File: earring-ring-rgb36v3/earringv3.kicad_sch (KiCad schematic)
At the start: 58 parts, among them J1 Conn_01x05, Q1 AO3401A, SW1 SW_Push, SW2 SW_Push, U1 GMA2718H09-F42-4P, U2 STM32L031G6Ux

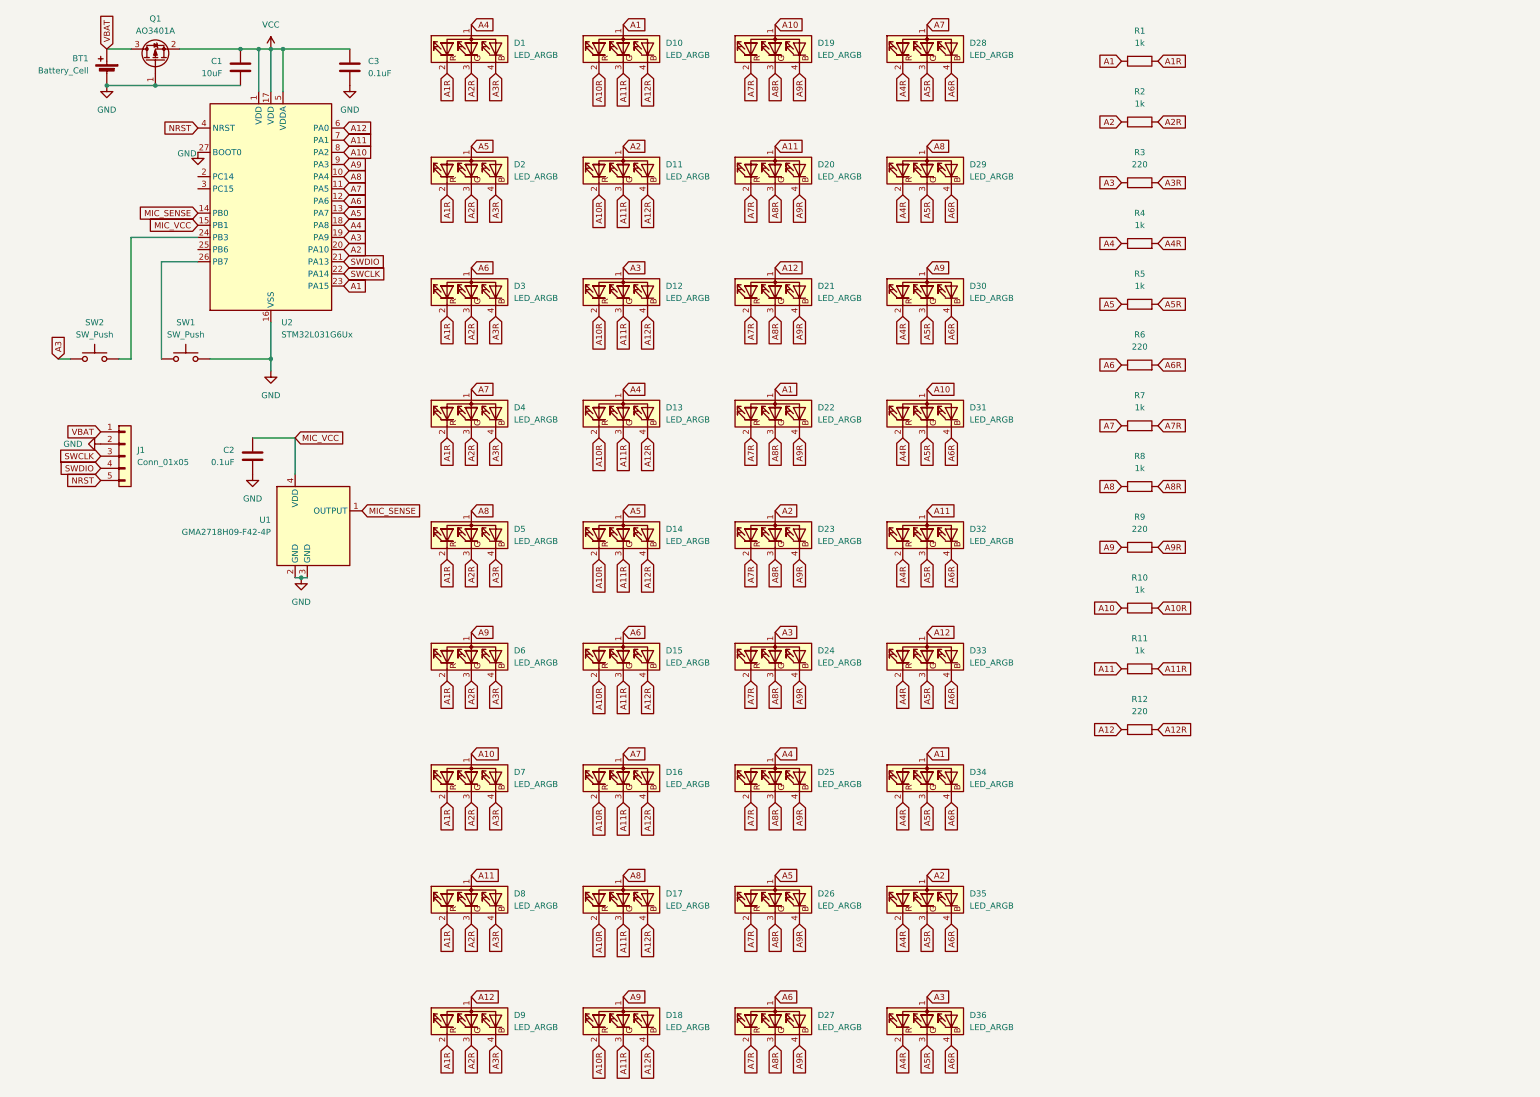
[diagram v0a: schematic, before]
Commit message: earring-ring-rgb36v3: schematic design for charlieplexing
This is the 3rd or 4th attempt, but the current schematic finally looks
usable.
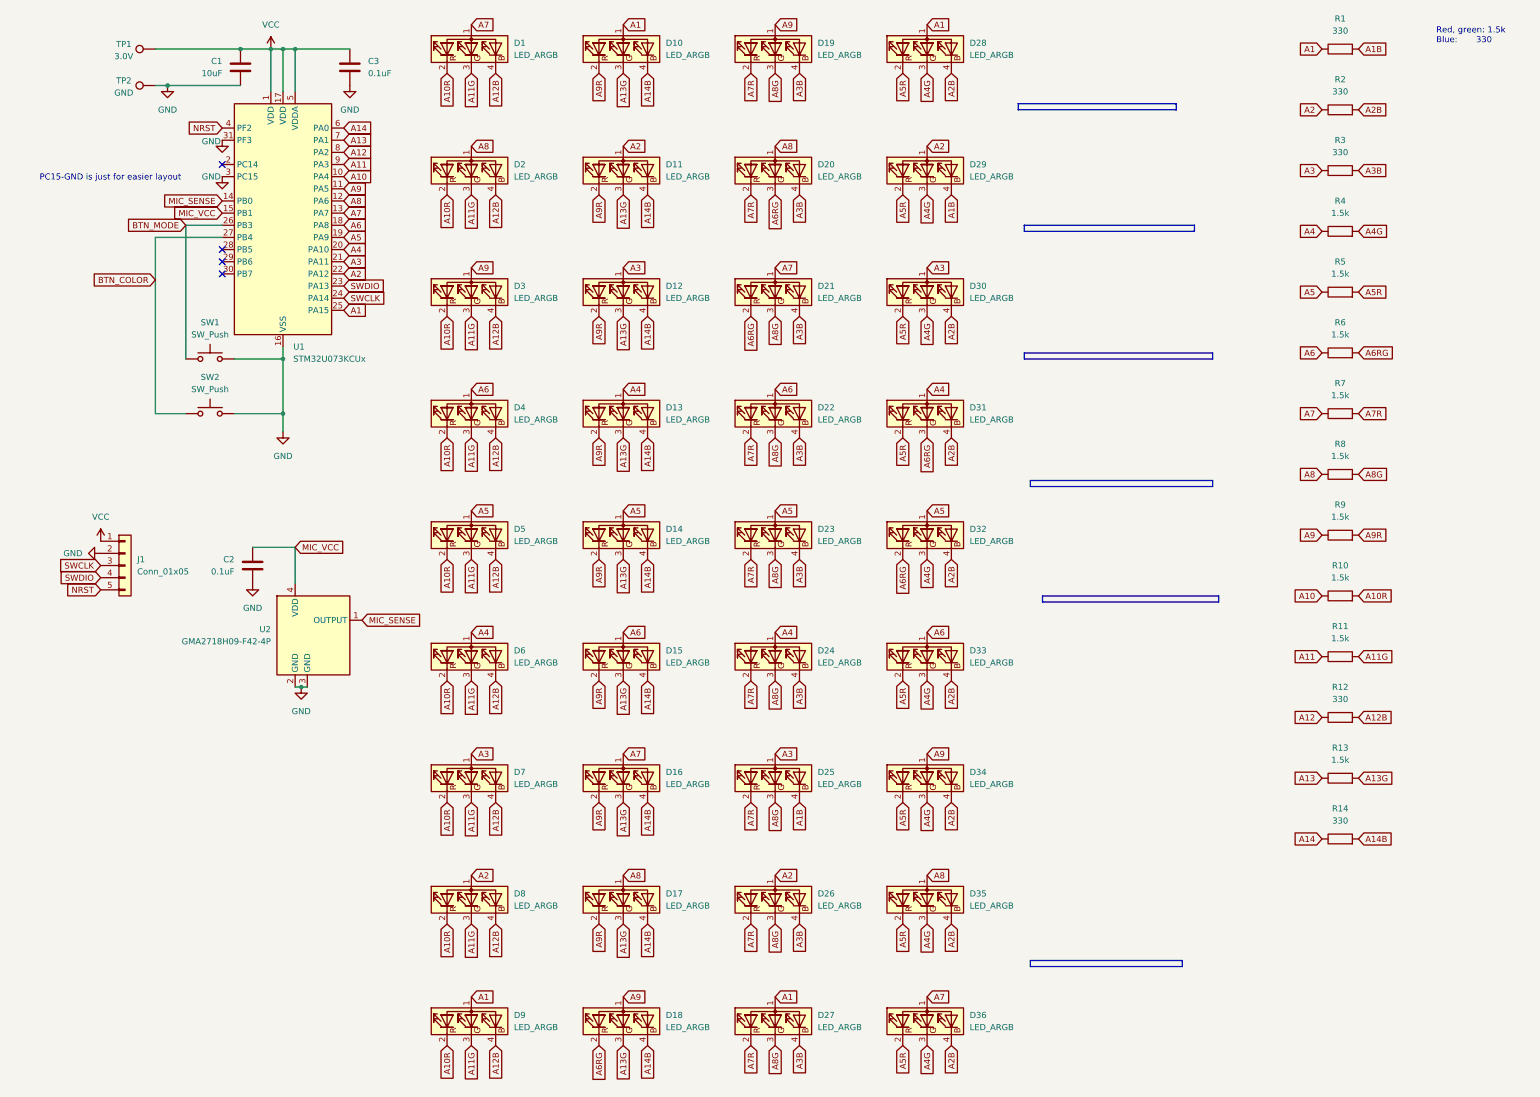
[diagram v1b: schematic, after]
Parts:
- removed BT1: Battery_Cell, Custom:MY-1220-03, symbol Device:Battery_Cell
- removed Q1: AO3401A, Package_TO_SOT_SMD:SOT-23, symbol Transistor_FET:AO3401A
- removed U2: STM32L031G6Ux, Package_DFN_QFN:QFN-28_4x4mm_P0.5mm, symbol MCU_ST_STM32L0:STM32L031G6Ux
- added R13: 1.5k, Resistor_SMD:R_0402_1005Metric, symbol Device:R
- added R14: 330, Resistor_SMD:R_0402_1005Metric, symbol Device:R
- added TP1: 3.0V, TestPoint:TestPoint_Pad_1.5x1.5mm, symbol Connector:TestPoint
- added TP2: GND, TestPoint:TestPoint_Pad_1.5x1.5mm, symbol Connector:TestPoint
- added U1: STM32U073KCUx, Package_DFN_QFN:QFN-32-1EP_5x5mm_P0.5mm_EP3.45x3.45mm, symbol MCU_ST_STM32U0:STM32U073KCUx
- R1, R2: value 1k -> 330; LCSC C11702 -> C25104
- R10, R11, R4, R5, R7, R8: value 1k -> 1.5k; LCSC C11702 -> C25867
- R12, R3: value 220 -> 330; LCSC C25091 -> C25104
- R6, R9: value 220 -> 1.5k; LCSC C25091 -> C25867
- renumbered U1 to U2
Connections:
- net VBAT is gone; now on net VCC: J1.1 (Pin_1)
- net A1: now also D27.1 (A), D28.1 (A), D9.1 (A), R1.1, U1.25 (PA15); no longer D22.1 (A), D34.1 (A), R1.2
- net A10: now also U1.10 (PA4); no longer D19.1 (A), D31.1 (A), D7.1 (A)
- net A10R: now also D1.2 (RK), D2.2 (RK), D3.2 (RK), D4.2 (RK), D5.2 (RK), D6.2 (RK), D7.2 (RK), D8.2 (RK), D9.2 (RK); no longer D10.2 (RK), D11.2 (RK), D12.2 (RK), D13.2 (RK), D14.2 (RK), D15.2 (RK), D16.2 (RK), D17.2 (RK), D18.2 (RK)
- net A11: now also U1.9 (PA3); no longer D20.1 (A), D32.1 (A), D8.1 (A)
- net A12: now also U1.8 (PA2); no longer D21.1 (A), D33.1 (A), D9.1 (A)
- net A2: now also D26.1 (A), D29.1 (A), D8.1 (A), U1.22 (PA12); no longer D23.1 (A), D35.1 (A)
- net A3: now also D25.1 (A), D30.1 (A), D7.1 (A), U1.21 (PA11); no longer D24.1 (A), D36.1 (A), SW2.1
- net A4: now also D24.1 (A), D31.1 (A), D6.1 (A), U1.20 (PA10); no longer D1.1 (A), D25.1 (A)
- net A5: now also D23.1 (A), D32.1 (A), D5.1 (A), U1.19 (PA9); no longer D2.1 (A), D26.1 (A)
- net A5R: now also D28.2 (RK), D29.2 (RK), D30.2 (RK), D31.2 (RK), D33.2 (RK), D34.2 (RK), D35.2 (RK), D36.2 (RK); no longer D28.3 (GK), D29.3 (GK), D30.3 (GK), D31.3 (GK), D32.3 (GK), D33.3 (GK), D34.3 (GK), D35.3 (GK), D36.3 (GK)
- net A6: now also D22.1 (A), D33.1 (A), D4.1 (A), U1.18 (PA8); no longer D27.1 (A), D3.1 (A)
- net A7: now also D1.1 (A), D21.1 (A), D36.1 (A), U1.13 (PA7); no longer D28.1 (A), D4.1 (A)
- net A7R: no longer D21.2 (RK)
- net A8: now also D2.1 (A), D20.1 (A), D35.1 (A), U1.12 (PA6); no longer D29.1 (A), D5.1 (A)
- net A9: now also D19.1 (A), D3.1 (A), D34.1 (A), U1.11 (PA5); no longer D30.1 (A), D6.1 (A)
- net A9R: now also D10.2 (RK), D11.2 (RK), D12.2 (RK), D13.2 (RK), D14.2 (RK), D15.2 (RK), D16.2 (RK), D17.2 (RK); no longer D19.4 (BK), D20.4 (BK), D21.4 (BK), D22.4 (BK), D23.4 (BK), D24.4 (BK), D25.4 (BK), D26.4 (BK), D27.4 (BK)
- net GND: now also SW2.1, TP2.1, U1.16 (VSS), U1.3 (PC15), U1.31 (PF3), U1.32 (VSS), U1.33 (VSS)
- net MIC_SENSE: now also U1.14 (PB0)
- net MIC_VCC: now also U1.15 (PB1)
- net NRST: now also U1.4 (PF2)
- net SWCLK: now also U1.24 (PA14)
- net SWDIO: now also U1.23 (PA13)
- net VCC: now also TP1.1, U1.1 (VDD), U1.17 (VDD), U1.5 (VDDA)
- net BTN_COLOR: now reaches SW2.2
- net BTN_COLOR: now also U1.27 (PB4)
- net BTN_MODE: now reaches SW1.2
- net BTN_MODE: now also U1.26 (PB3)
- net A11R renamed A13G
- net A13G: now also R13.2; no longer R11.2
- net A12R renamed A14B
- net A14B: now also R14.2; no longer R12.2
- removed net A1R: D1.2 (RK), D2.2 (RK), D3.2 (RK), D4.2 (RK), D5.2 (RK), D6.2 (RK), D7.2 (RK), D8.2 (RK), D9.2 (RK), R1.1
- net A2R renamed A11G
- net A11G: now also R11.2; no longer R2.2
- net A3R renamed A12B
- net A12B: now also R12.2; no longer R3.2
- removed net A4R: D28.2 (RK), D29.2 (RK), D30.2 (RK), D31.2 (RK), D32.2 (RK), D33.2 (RK), D34.2 (RK), D35.2 (RK), D36.2 (RK), R4.2
- net A6R renamed A2B
- net A2B: now also R2.2; no longer D29.4 (BK), R6.2
- net A8R renamed A8G
- net A8G: no longer D20.3 (GK)
- new net A13: R13.1, U1.7 (PA1)
- new net A14: R14.1, U1.6 (PA0)
- new net A1B: D25.4 (BK), D29.4 (BK), R1.2
- new net A3B: D19.4 (BK), D20.4 (BK), D21.4 (BK), D22.4 (BK), D23.4 (BK), D24.4 (BK), D26.4 (BK), D27.4 (BK), R3.2
- new net A4G: D28.3 (GK), D29.3 (GK), D30.3 (GK), D32.3 (GK), D33.3 (GK), D34.3 (GK), D35.3 (GK), D36.3 (GK), R4.2
- new net A6RG: D18.2 (RK), D20.3 (GK), D21.2 (RK), D31.3 (GK), D32.2 (RK), R6.2
- no-connect marks 0 -> 4
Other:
- note added: "PC15-GND is just for easier layout"
- note added: "Red, green: 1.5k Blue: 330"
- moved on the sheet: C2, J1, SW1, SW2, U2

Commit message: earring-ring-rgb36v3: prepare for prototype production
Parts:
- SW1: LCSC C561519 -> C720477
- SW2: LCSC (none) -> C720477
- TP1, TP2: now left out of the parts list
- U1: LCSC (none) -> C22445363
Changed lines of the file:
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@@
 		)
 		(instances
-			(project "earring"
+			(project "earringv3"
 				(path "/5b672b97-2486-4be1-9927-7141d9b63fb2"
 					(reference "D13")
@@
 		)
 		(instances
-			(project "earring"
+			(project "earringv3"
 				(path "/5b672b97-2486-4be1-9927-7141d9b63fb2"
 					(reference "D30")
@@
 		)
 		(instances
-			(project "earring"
+			(project "earringv3"
 				(path "/5b672b97-2486-4be1-9927-7141d9b63fb2"
 					(reference "D24")
@@
 		)
 		(instances
-			(project "earring"
+			(project "earringv3"
 				(path "/5b672b97-2486-4be1-9927-7141d9b63fb2"
 					(reference "D31")
@@
 		)
 		(instances
-			(project "earring"
+			(project "earringv3"
 				(path "/5b672b97-2486-4be1-9927-7141d9b63fb2"
 					(reference "D18")
@@
 		)
 		(instances
-			(project "earring"
+			(project "earringv3"
 				(path "/5b672b97-2486-4be1-9927-7141d9b63fb2"
 					(reference "D6")
@@
 		)
 		(instances
-			(project "earring"
+			(project "earringv3"
 				(path "/5b672b97-2486-4be1-9927-7141d9b63fb2"
 					(reference "D34")
@@
 		)
 		(instances
-			(project "earring"
+			(project "earringv3"
 				(path "/5b672b97-2486-4be1-9927-7141d9b63fb2"
 					(reference "C2")
@@
 		)
 		(instances
-			(project "earring"
+			(project "earringv3"
 				(path "/5b672b97-2486-4be1-9927-7141d9b63fb2"
 					(reference "D19")
@@
 			)
 		)
+		(property "LCSC" "C22445363"
+			(at 66.04 59.69 0)
+			(effects
+				(font
+					(size 1.27 1.27)
+				)
+				(hide yes)
+			)
+		)
 		(pin "24"
 		)
@@
 		)
 		(instances
-			(project ""
+			(project "earringv3"
 				(path "/5b672b97-2486-4be1-9927-7141d9b63fb2"
 					(reference "U1")
@@
 			)
 		)
+		(property "LCSC" "C720477"
+			(at 50.8 99.06 0)
+			(effects
+				(font
+					(size 1.27 1.27)
+				)
+				(hide yes)
+			)
+		)
 		(pin "1"
 		)
@@
 		)
 		(instances
-			(project "earring"
+			(project "earringv3"
 				(path "/5b672b97-2486-4be1-9927-7141d9b63fb2"
 					(reference "SW2")
@@
 		)
 		(instances
-			(project "earring"
+			(project "earringv3"
 				(path "/5b672b97-2486-4be1-9927-7141d9b63fb2"
 					(reference "D3")
@@
 		)
 		(instances
-			(project "earring"
+			(project "earringv3"
 				(path "/5b672b97-2486-4be1-9927-7141d9b63fb2"
 					(reference "D23")
@@
 		)
 		(instances
-			(project "earring"
+			(project "earringv3"
 				(path "/5b672b97-2486-4be1-9927-7141d9b63fb2"
 					(reference "D16")
@@
 		)
 		(instances
-			(project ""
+			(project "earringv3"
 				(path "/5b672b97-2486-4be1-9927-7141d9b63fb2"
 					(reference "#PWR05")
@@
 		)
 		(instances
-			(project "earring"
+			(project "earringv3"
 				(path "/5b672b97-2486-4be1-9927-7141d9b63fb2"
 					(reference "#PWR03")
@@
 		)
 		(instances
-			(project "earring"
+			(project "earringv3"
 				(path "/5b672b97-2486-4be1-9927-7141d9b63fb2"
 					(reference "#PWR08")
@@
 		)
 		(instances
-			(project ""
+			(project "earringv3"
 				(path "/5b672b97-2486-4be1-9927-7141d9b63fb2"
 					(reference "#PWR04")
@@
 		)
 		(instances
-			(project "earring"
+			(project "earringv3"
 				(path "/5b672b97-2486-4be1-9927-7141d9b63fb2"
 					(reference "D2")
@@
 		)
 		(instances
-			(project "earring"
+			(project "earringv3"
 				(path "/5b672b97-2486-4be1-9927-7141d9b63fb2"
 					(reference "D15")
@@
 		)
 		(instances
-			(project "earring"
+			(project "earringv3"
 				(path "/5b672b97-2486-4be1-9927-7141d9b63fb2"
 					(reference "D22")
@@
 		(unit 1)
 		(exclude_from_sim no)
-		(in_bom yes)
+		(in_bom no)
 		(on_board yes)
 		(dnp no)
@@
 		)
 		(instances
-			(project "earring"
+			(project "earringv3"
 				(path "/5b672b97-2486-4be1-9927-7141d9b63fb2"
 					(reference "D26")
@@
 		)
 		(instances
-			(project "earring"
+			(project "earringv3"
 				(path "/5b672b97-2486-4be1-9927-7141d9b63fb2"
 					(reference "D7")
@@
 		)
 		(instances
-			(project "earring"
+			(project "earringv3"
 				(path "/5b672b97-2486-4be1-9927-7141d9b63fb2"
 					(reference "D27")
@@
 		)
 		(instances
-			(project "earring"
+			(project "earringv3"
 				(path "/5b672b97-2486-4be1-9927-7141d9b63fb2"
 					(reference "D21")
@@
 		)
 		(instances
-			(project "earring"
+			(project "earringv3"
 				(path "/5b672b97-2486-4be1-9927-7141d9b63fb2"
 					(reference "D9")
@@
 		(unit 1)
 		(exclude_from_sim no)
-		(in_bom yes)
+		(in_bom no)
 		(on_board yes)
 		(dnp no)
@@
 		)
 		(instances
-			(project "earring"
+			(project "earringv3"
 				(path "/5b672b97-2486-4be1-9927-7141d9b63fb2"
 					(reference "D5")
@@
 		)
 		(instances
-			(project "earring"
+			(project "earringv3"
 				(path "/5b672b97-2486-4be1-9927-7141d9b63fb2"
 					(reference "D12")
@@
 		)
 		(instances
-			(project "earring"
+			(project "earringv3"
 				(path "/5b672b97-2486-4be1-9927-7141d9b63fb2"
 					(reference "D25")
@@
 		)
 		(instances
-			(project "earring"
+			(project "earringv3"
 				(path "/5b672b97-2486-4be1-9927-7141d9b63fb2"
 					(reference "C1")
@@
 		)
 		(instances
-			(project "earring"
+			(project "earringv3"
 				(path "/5b672b97-2486-4be1-9927-7141d9b63fb2"
 					(reference "D11")
@@
 		)
 		(instances
-			(project "earring"
+			(project "earringv3"
 				(path "/5b672b97-2486-4be1-9927-7141d9b63fb2"
 					(reference "D36")
@@
 		)
 		(instances
-			(project "earring"
+			(project "earringv3"
 				(path "/5b672b97-2486-4be1-9927-7141d9b63fb2"
 					(reference "D10")
@@
 		)
 		(instances
-			(project "earring"
+			(project "earringv3"
 				(path "/5b672b97-2486-4be1-9927-7141d9b63fb2"
 					(reference "D17")
@@
 		)
 		(instances
-			(project ""
+			(project "earringv3"
 				(path "/5b672b97-2486-4be1-9927-7141d9b63fb2"
 					(reference "D1")
@@
 		)
 		(instances
-			(project "earring"
+			(project "earringv3"
 				(path "/5b672b97-2486-4be1-9927-7141d9b63fb2"
 					(reference "#PWR06")
@@
 		)
 		(instances
-			(project "earring"
+			(project "earringv3"
 				(path "/5b672b97-2486-4be1-9927-7141d9b63fb2"
 					(reference "D20")
@@
 		)
 		(instances
-			(project "earring"
+			(project "earringv3"
 				(path "/5b672b97-2486-4be1-9927-7141d9b63fb2"
 					(reference "D4")
@@
 		)
 		(instances
-			(project "earring"
+			(project "earringv3"
 				(path "/5b672b97-2486-4be1-9927-7141d9b63fb2"
 					(reference "D8")
@@
 		)
 		(instances
-			(project ""
+			(project "earringv3"
 				(path "/5b672b97-2486-4be1-9927-7141d9b63fb2"
 					(reference "J1")
@@
 		)
 		(instances
-			(project "earring"
+			(project "earringv3"
 				(path "/5b672b97-2486-4be1-9927-7141d9b63fb2"
 					(reference "D35")
@@
 		)
 		(instances
-			(project "earring"
+			(project "earringv3"
 				(path "/5b672b97-2486-4be1-9927-7141d9b63fb2"
 					(reference "D33")
@@
 		)
 		(instances
-			(project ""
+			(project "earringv3"
 				(path "/5b672b97-2486-4be1-9927-7141d9b63fb2"
 					(reference "U2")
@@
 		)
 		(instances
-			(project "earring"
+			(project "earringv3"
 				(path "/5b672b97-2486-4be1-9927-7141d9b63fb2"
 					(reference "D14")
@@
 		)
 		(instances
-			(project "earring"
+			(project "earringv3"
 				(path "/5b672b97-2486-4be1-9927-7141d9b63fb2"
 					(reference "D32")
@@
 		)
 		(instances
-			(project "earring"
+			(project "earringv3"
 				(path "/5b672b97-2486-4be1-9927-7141d9b63fb2"
 					(reference "D28")
@@
 		)
 		(instances
-			(project "earring"
+			(project "earringv3"
 				(path "/5b672b97-2486-4be1-9927-7141d9b63fb2"
 					(reference "#PWR02")
@@
 			)
 		)
-		(property "LCSC" "C561519"
+		(property "LCSC" "C720477"
 			(at 50.8 87.63 0)
 			(effects
@@
 		)
 		(instances
-			(project "earring"
+			(project "earringv3"
 				(path "/5b672b97-2486-4be1-9927-7141d9b63fb2"
 					(reference "SW1")
@@
 		)
 		(instances
-			(project "earring"
+			(project "earringv3"
 				(path "/5b672b97-2486-4be1-9927-7141d9b63fb2"
 					(reference "#PWR01")
@@
 		)
 		(instances
-			(project "earring"
+			(project "earringv3"
 				(path "/5b672b97-2486-4be1-9927-7141d9b63fb2"
 					(reference "D29")
@@
 		)
 		(instances
-			(project "earring"
+			(project "earringv3"
 				(path "/5b672b97-2486-4be1-9927-7141d9b63fb2"
 					(reference "C3")
